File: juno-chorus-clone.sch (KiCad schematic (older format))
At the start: 168 parts, among them P1 15VAC_IN, P2 AUDIO_IN, P3 AUDIO_OUT_1, P4 AUDIO_OUT_2, Q1 2SC1815, Q10 2SC1815, Q11 2SA1015, Q12 2SA1015, Q13 2SC1815, Q14 2SA1015, Q15 2SA1015, Q16 2SK30, Q17 2SK30, Q18 2SA1015, Q19 2SA1015, Q2 2SC1815, Q3 2SA1015, Q4 2SA1015, Q5 2SC1815, Q6 2SC1815, Q7 2SA1015, Q8 2SA1015, Q9 2SC1815, SW1 SW_PUSH, U1 TL082, U10 TL082, U2 LM7815CT, U3 LM7915CT, U4 TL082, U5 MN3009, U6 MN3101, U7 MN3009, U8 MN3101, U9 TL082

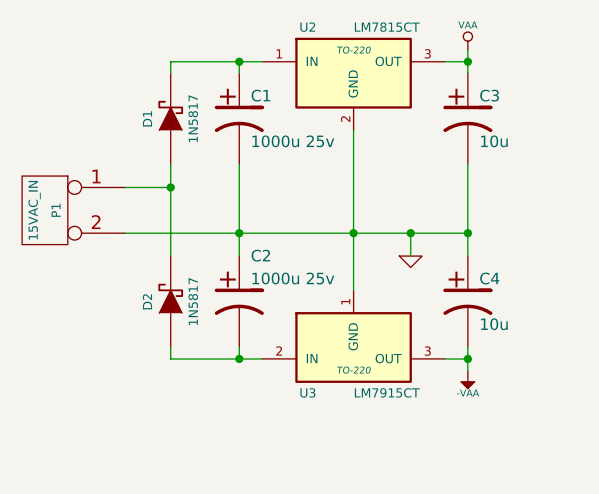
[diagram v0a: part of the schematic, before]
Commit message: 1N5817 -> 1N5819 (1N5817 can't handle 15VAC)
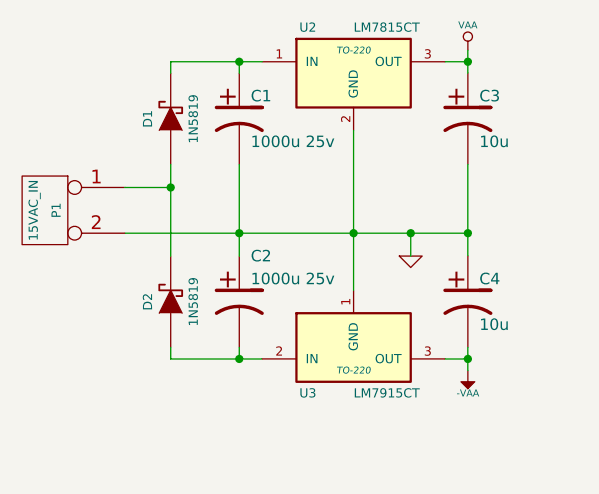
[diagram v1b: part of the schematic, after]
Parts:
- D1, D2: value 1N5817 -> 1N5819
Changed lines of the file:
@@
 Sheet 1 1
 Title "Roland Juno-60 chorus board clone"
-Date "7 may 2014"
+Date "12 sep 2015"
 Rev "4"
 Comp "GliGli's DIY"
@@
 P 1350 1000
 F 0 "D1" H 1350 1100 40  0000 C CNN
-F 1 "1N5817" H 1350 900 40  0000 C CNN
+F 1 "1N5819" H 1350 900 40  0000 C CNN
 F 2 "~" H 1350 1000 60  0000 C CNN
 F 3 "~" H 1350 1000 60  0000 C CNN
@@
 P 1350 1800
 F 0 "D2" H 1350 1900 40  0000 C CNN
-F 1 "1N5817" H 1350 1700 40  0000 C CNN
+F 1 "1N5819" H 1350 1700 40  0000 C CNN
 F 2 "~" H 1350 1800 60  0000 C CNN
 F 3 "~" H 1350 1800 60  0000 C CNN
